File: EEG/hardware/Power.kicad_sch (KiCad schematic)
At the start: 16 parts, among them J2 2S_BATTERY, J4 POWER_ENABLE, U3 AP63203WU-7, U4 LP2985AIM5-5.0/NOPB

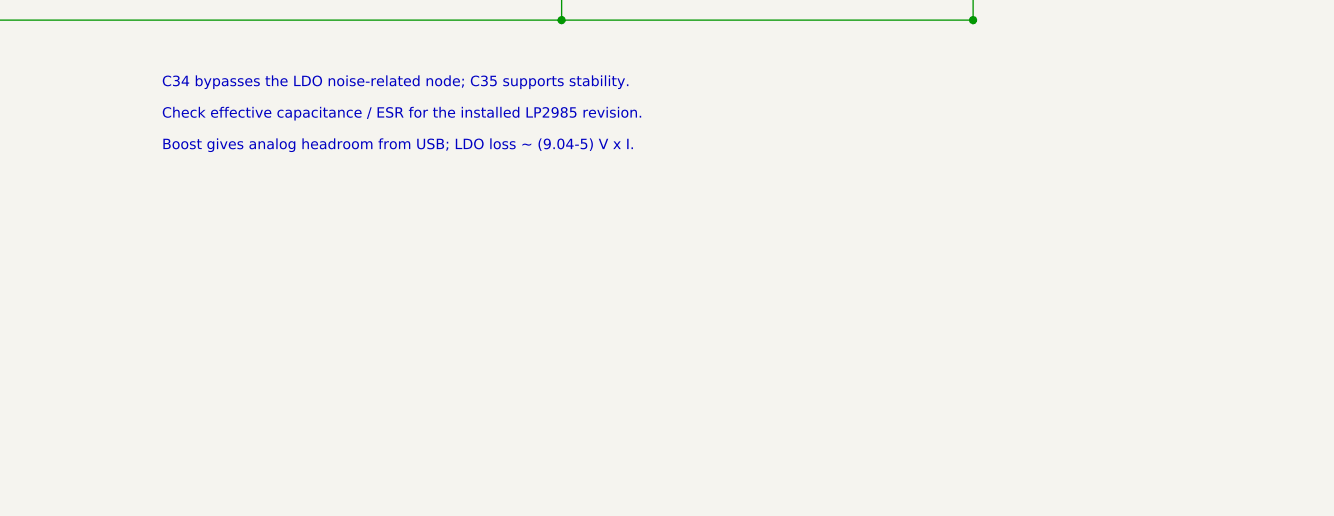
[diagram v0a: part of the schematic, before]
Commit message: feat(eeg): compact and center PCB, add power LED
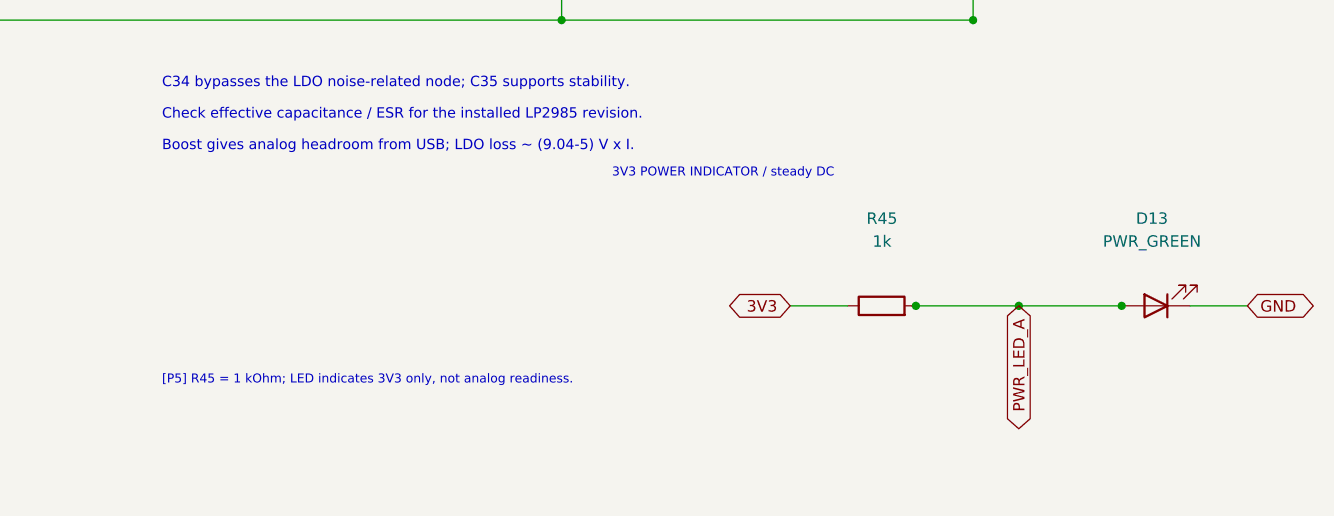
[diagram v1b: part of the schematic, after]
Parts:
- added D13: PWR_GREEN, LED_SMD:LED_0805_2012Metric, symbol Device:LED
- added R45: 1k, Resistor_SMD:R_0805_2012Metric, symbol Device:R
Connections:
- net 3V3: now also R45.1
- net GND: now also D13.1 (K)
- new net PWR_LED_A: D13.2 (A), R45.2
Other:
- note added: "3V3 POWER INDICATOR / steady DC"
- note added: "[P5] R45 = 1 kOhm; LED indicates 3V3 only, not analog readiness."
